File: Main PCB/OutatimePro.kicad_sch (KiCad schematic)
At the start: 42 parts, among them IC1 PAM8904JPR, J1 USB_B_Micro_PCB_Edge_receptac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, J2 FH35C-9S-0.3SHW, J3 TagConnect_TC2030-NL, Q1 ALS-PT19-315C/L177/TR8, SW1 EVPAWED40, U1 ATSAML22N18A-CFUT, U2 MIC5365-3.3YMT, U3 USBLC6-2P6, U4 MAX40200ANS, Y1 32.768kHz

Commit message: v270826: change programming header, add test points
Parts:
- removed J3: TagConnect_TC2030-NL, Connector:Tag-Connect_TC2030-IDC-NL_2x03_P1.27mm_Vertical, symbol Connector:Conn_ARM_SWD_TagConnect_TC2030-NL
- added J3: OSO_SWD, OutatimePro:OSO_SWD_2x3, symbol OutatimePro:OSO_SWD
- added TP1: USB+, OutatimePro:TestPoint_Pad_D1.5mm, symbol Connector:TestPoint_Alt
- added TP2: USB-, OutatimePro:TestPoint_Pad_D1.5mm, symbol Connector:TestPoint_Alt
- added TP3: +3v3, OutatimePro:TestPoint_Pad_D1.5mm, symbol Connector:TestPoint_Alt
- added TP4: GND, OutatimePro:TestPoint_Pad_D1.5mm, symbol Connector:TestPoint_Alt
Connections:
- net +3.3V: now also TP3.1
- net GND: now also J3.2 (GND), TP4.1
- net SWCLK: now also J3.4 (SWCLK)
- net SWDIO: now also J3.1 (SWDIO)
- net VCC: now also J3.3 (VCC)
- net ~{RESET}: now also J3.5 (~{RESET})
- net at J1.2 (D-), U3.3 (I/O2): now also TP2.1
- net at J1.3 (D+), U3.1 (I/O1): now also TP1.1
- no-connect marks 3 -> 2

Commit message: move test pads to a good location
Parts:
- TP1, TP2, TP3, TP4: footprint OutatimePro:TestPoint_Pad_D1.5mm -> OutatimePro:TestPoint_Pad_D0.75mm
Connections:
- net +3.3V: no longer TP3.1
- net USB_N: now also TP2.1
- net USB_P: now also TP1.1
- net VCC: now also TP3.1
- net at J1.3 (D+), U3.1 (I/O1): no longer TP1.1
- net at J1.2 (D-), U3.3 (I/O2): no longer TP2.1
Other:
- moved on the sheet: TP1, TP2, TP3
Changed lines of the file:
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@@
 	)
 	(junction
+		(at 133.35 38.1)
+		(diameter 0)
+		(color 0 0 0 0)
+	)
+	(junction
 		(at 114.3 128.27)
 		(diameter 0)
@@
 	)
 	(junction
-		(at 133.35 38.1)
-		(diameter 0)
-		(color 0 0 0 0)
-	)
-	(junction
 		(at 114.3 133.35)
 		(diameter 0)
@@
 	)
 	(junction
-		(at 91.44 55.88)
-		(diameter 0)
-		(color 0 0 0 0)
-	)
-	(junction
 		(at 91.44 38.1)
 		(diameter 0)
@@
 	)
 	(junction
-		(at 100.33 78.74)
-		(diameter 0)
-		(color 0 0 0 0)
-	)
-	(junction
 		(at 59.69 55.88)
 		(diameter 0)
@@
 	)
 	(junction
-		(at 100.33 81.28)
-		(diameter 0)
-		(color 0 0 0 0)
-	)
-	(junction
 		(at 271.78 24.13)
 		(diameter 0)
@@
 	(wire
 		(pts
-			(xy 100.33 78.74) (xy 139.7 78.74)
-		)
-		(stroke
-			(width 0)
-			(type default)
-		)
-	)
-	(wire
-		(pts
 			(xy 388.62 231.14) (xy 391.16 231.14)
 		)
@@
 	(wire
 		(pts
-			(xy 149.86 81.28) (xy 160.02 81.28)
+			(xy 149.86 81.28) (xy 168.91 81.28)
 		)
 		(stroke
@@
 	(wire
 		(pts
-			(xy 41.91 78.74) (xy 100.33 78.74)
+			(xy 41.91 78.74) (xy 139.7 78.74)
 		)
 		(stroke
@@
 	(wire
 		(pts
-			(xy 149.86 78.74) (xy 160.02 78.74)
+			(xy 149.86 78.74) (xy 168.91 78.74)
 		)
 		(stroke
@@
 	(wire
 		(pts
-			(xy 100.33 81.28) (xy 139.7 81.28)
-		)
-		(stroke
-			(width 0)
-			(type default)
-		)
-	)
-	(wire
-		(pts
 			(xy 91.44 153.67) (xy 116.84 153.67)
 		)
@@
 	(wire
 		(pts
-			(xy 41.91 81.28) (xy 100.33 81.28)
+			(xy 41.91 81.28) (xy 139.7 81.28)
 		)
 		(stroke
@@
 	(symbol
 		(lib_id "Connector:TestPoint_Alt")
-		(at 100.33 78.74 0)
+		(at 168.91 78.74 0)
 		(unit 1)
 		(body_style 1)
@@
 		(fields_autoplaced yes)
 		(property "Reference" "TP1"
-			(at 102.87 74.1679 0)
+			(at 171.45 74.1679 0)
 			(show_name no)
 			(do_not_autoplace no)
@@
 		)
 		(property "Value" "USB+"
-			(at 102.87 76.7079 0)
+			(at 171.45 76.7079 0)
 			(show_name no)
 			(do_not_autoplace no)
@@
 			)
 		)
-		(property "Footprint" "OutatimePro:TestPoint_Pad_D1.5mm"
-			(at 105.41 78.74 0)
+		(property "Footprint" "OutatimePro:TestPoint_Pad_D0.75mm"
+			(at 173.99 78.74 0)
 			(hide yes)
 			(show_name no)
@@
 		)
 		(property "Datasheet" ""
-			(at 105.41 78.74 0)
+			(at 173.99 78.74 0)
 			(hide yes)
 			(show_name no)
@@
 		)
 		(property "Description" "test point (alternative shape)"
-			(at 100.33 78.74 0)
+			(at 168.91 78.74 0)
 			(hide yes)
 			(show_name no)
@@
 	(symbol
 		(lib_id "Connector:TestPoint_Alt")
-		(at 100.33 81.28 0)
+		(at 168.91 81.28 0)
 		(mirror x)
 		(unit 1)
@@
 		(dnp no)
 		(property "Reference" "TP2"
-			(at 102.87 85.8521 0)
+			(at 171.45 85.8521 0)
 			(show_name no)
 			(do_not_autoplace no)
@@
 		)
 		(property "Value" "USB-"
-			(at 102.87 83.3121 0)
+			(at 171.45 83.3121 0)
 			(show_name no)
 			(do_not_autoplace no)
@@
 			)
 		)
-		(property "Footprint" "OutatimePro:TestPoint_Pad_D1.5mm"
-			(at 105.41 81.28 0)
+		(property "Footprint" "OutatimePro:TestPoint_Pad_D0.75mm"
+			(at 173.99 81.28 0)
 			(hide yes)
 			(show_name no)
@@
 		)
 		(property "Datasheet" ""
-			(at 105.41 81.28 0)
+			(at 173.99 81.28 0)
 			(hide yes)
 			(show_name no)
@@
 		)
 		(property "Description" "test point (alternative shape)"
-			(at 100.33 81.28 0)
+			(at 168.91 81.28 0)
 			(hide yes)
 			(show_name no)
@@
 			)
 		)
-		(property "Footprint" "OutatimePro:TestPoint_Pad_D1.5mm"
+		(property "Footprint" "OutatimePro:TestPoint_Pad_D0.75mm"
 			(at 45.72 90.17 0)
 			(hide yes)
@@
 	(symbol
 		(lib_id "Connector:TestPoint_Alt")
-		(at 91.44 55.88 0)
+		(at 135.89 38.1 0)
 		(mirror x)
 		(unit 1)
@@
 		(fields_autoplaced yes)
 		(property "Reference" "TP3"
-			(at 88.9 57.9119 0)
+			(at 133.35 40.1319 0)
 			(show_name no)
 			(do_not_autoplace no)
@@
 		)
 		(property "Value" "+3v3"
-			(at 88.9 60.4519 0)
+			(at 133.35 42.6719 0)
 			(show_name no)
 			(do_not_autoplace no)
@@
 			)
 		)
-		(property "Footprint" "OutatimePro:TestPoint_Pad_D1.5mm"
-			(at 96.52 55.88 0)
+		(property "Footprint" "OutatimePro:TestPoint_Pad_D0.75mm"
+			(at 140.97 38.1 0)
 			(hide yes)
 			(show_name no)
@@
 		)
 		(property "Datasheet" ""
-			(at 96.52 55.88 0)
+			(at 140.97 38.1 0)
 			(hide yes)
 			(show_name no)
@@
 		)
 		(property "Description" "test point (alternative shape)"
-			(at 91.44 55.88 0)
+			(at 135.89 38.1 0)
 			(hide yes)
 			(show_name no)

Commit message: move test pads more and change version format
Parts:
- TP1, TP2, TP3, TP4: footprint OutatimePro:TestPoint_Pad_D0.75mm -> OutatimePro:TestPoint_Pad_D1.0mm
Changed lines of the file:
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@@
 			)
 		)
-		(property "Footprint" "OutatimePro:TestPoint_Pad_D0.75mm"
+		(property "Footprint" "OutatimePro:TestPoint_Pad_D1.0mm"
 			(at 173.99 78.74 0)
 			(hide yes)
@@
 			)
 		)
-		(property "Footprint" "OutatimePro:TestPoint_Pad_D0.75mm"
+		(property "Footprint" "OutatimePro:TestPoint_Pad_D1.0mm"
 			(at 173.99 81.28 0)
 			(hide yes)
@@
 			)
 		)
-		(property "Footprint" "OutatimePro:TestPoint_Pad_D0.75mm"
+		(property "Footprint" "OutatimePro:TestPoint_Pad_D1.0mm"
 			(at 45.72 90.17 0)
 			(hide yes)
@@
 			)
 		)
-		(property "Footprint" "OutatimePro:TestPoint_Pad_D0.75mm"
+		(property "Footprint" "OutatimePro:TestPoint_Pad_D1.0mm"
 			(at 140.97 38.1 0)
 			(hide yes)

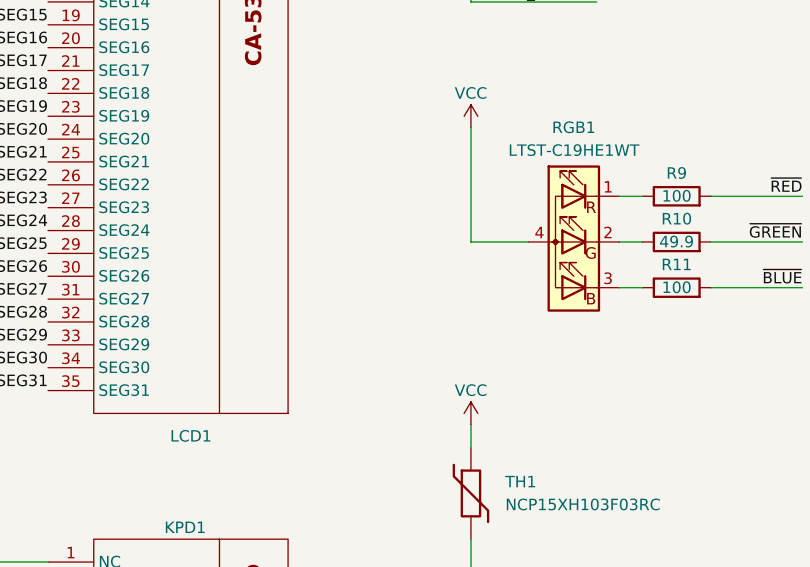
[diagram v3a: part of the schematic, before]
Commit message: resolve some drc errors, add cap to rgb led
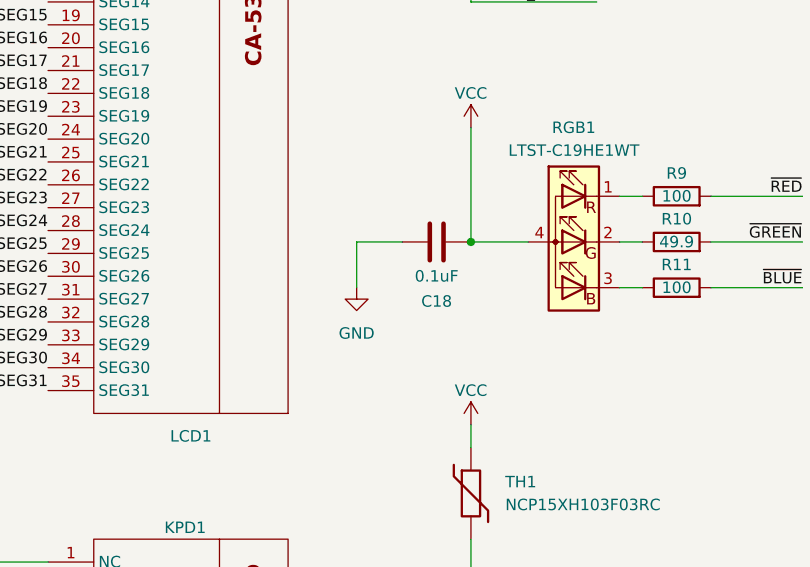
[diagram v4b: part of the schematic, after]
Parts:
- added C18: 0.1uF, Capacitor_SMD:C_0402_1005Metric, symbol Device:C
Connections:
- net GND: now also C18.1
- net VCC: now also C18.2
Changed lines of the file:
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@@
 	)
 	(junction
+		(at 336.55 134.62)
+		(diameter 0)
+		(color 0 0 0 0)
+	)
+	(junction
 		(at 114.3 142.24)
 		(diameter 0)
@@
 	(wire
 		(pts
+			(xy 323.85 134.62) (xy 323.85 139.7)
+		)
+		(stroke
+			(width 0)
+			(type default)
+		)
+	)
+	(wire
+		(pts
 			(xy 39.37 259.08) (xy 44.45 259.08)
 		)
@@
 	(wire
 		(pts
+			(xy 328.93 134.62) (xy 323.85 134.62)
+		)
+		(stroke
+			(width 0)
+			(type default)
+		)
+	)
+	(wire
+		(pts
 			(xy 114.3 130.81) (xy 114.3 133.35)
 		)
@@
 	)
 	(symbol
+		(lib_id "Device:C")
+		(at 332.74 134.62 90)
+		(mirror x)
+		(unit 1)
+		(body_style 1)
+		(exclude_from_sim no)
+		(in_bom yes)
+		(on_board yes)
+		(in_pos_files yes)
+		(dnp no)
+		(property "Reference" "C18"
+			(at 332.74 141.224 90)
+			(show_name no)
+			(do_not_autoplace no)
+			(effects
+				(font
+					(size 1.27 1.27)
+				)
+			)
+		)
+		(property "Value" "0.1uF"
+			(at 332.74 138.43 90)
+			(show_name no)
+			(do_not_autoplace no)
+			(effects
+				(font
+					(size 1.27 1.27)
+				)
+			)
+		)
+		(property "Footprint" "Capacitor_SMD:C_0402_1005Metric"
+			(at 336.55 135.5852 0)
+			(hide yes)
+			(show_name no)
+			(do_not_autoplace no)
+			(effects
+				(font
+					(size 1.27 1.27)
+				)
+			)
+		)
+		(property "Datasheet" ""
+			(at 332.74 134.62 0)
+			(hide yes)
+			(show_name no)
+			(do_not_autoplace no)
+			(effects
+				(font
+					(size 1.27 1.27)
+				)
+			)
+		)
+		(property "Description" "Unpolarized capacitor"
+			(at 332.74 134.62 0)
+			(hide yes)
+			(show_name no)
+			(do_not_autoplace no)
+			(effects
+				(font
+					(size 1.27 1.27)
+				)
+			)
+		)
+		(property "LCSC Part #" "C14663"
+			(at 332.74 134.62 90)
+			(hide yes)
+			(show_name no)
+			(do_not_autoplace no)
+			(effects
+				(font
+					(size 1.27 1.27)
+				)
+			)
+		)
+		(property "Max Height" ""
+			(at 332.74 134.62 90)
+			(hide yes)
+			(show_name no)
+			(do_not_autoplace no)
+			(effects
+				(font
+					(size 1.27 1.27)
+				)
+			)
+		)
+		(pin "1"
+		)
+		(pin "2"
+		)
+		(instances
+			(project "OutatimePro"
+				(path "/524ea2ee-4ba7-44dc-a60b-09b30277d096"
+					(reference "C18")
+					(unit 1)
+				)
+			)
+		)
+	)
+	(symbol
 		(lib_id "Device:R")
 		(at 264.16 30.48 0)
@@
 					(unit 1)
 				)
+			)
+		)
+	)
+	(symbol
+		(lib_id "power:GND")
+		(at 323.85 139.7 0)
+		(mirror y)
+		(unit 1)
+		(body_style 1)
+		(exclude_from_sim no)
+		(in_bom yes)
+		(on_board yes)
+		(in_pos_files yes)
+		(dnp no)
+		(fields_autoplaced yes)
+		(property "Reference" "#PWR038"
+			(at 323.85 146.05 0)
+			(hide yes)
+			(show_name no)
+			(do_not_autoplace no)
+			(effects
+				(font
+					(size 1.27 1.27)
+				)
+			)
+		)
+		(property "Value" "GND"
+			(at 323.85 144.78 0)
+			(show_name no)
+			(do_not_autoplace no)
+			(effects
+				(font
+					(size 1.27 1.27)
+				)
+			)
+		)
+		(property "Footprint" ""
+			(at 323.85 139.7 0)
+			(hide yes)
+			(show_name no)
+			(do_not_autoplace no)
+			(effects
+				(font
+					(size 1.27 1.27)
+				)
+			)
+		)
+		(property "Datasheet" ""
+			(at 323.85 139.7 0)
+			(hide yes)
+			(show_name no)
+			(do_not_autoplace no)
+			(effects
+				(font
+					(size 1.27 1.27)
+				)
+			)
+		)
+		(property "Description" "Power symbol creates a global label with name \"GND\" , ground"
+			(at 323.85 139.7 0)
+			(hide yes)
+			(show_name no)
+			(do_not_autoplace no)
+			(effects
+				(font
+					(size 1.27 1.27)
+				)
+			)
+		)
+		(pin "1"
+		)
+		(instances
+			(project "OutatimePro"
+				(path "/524ea2ee-4ba7-44dc-a60b-09b30277d096"
+					(reference "#PWR038")
+					(unit 1)
+				)
